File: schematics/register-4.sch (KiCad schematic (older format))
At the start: 0 parts

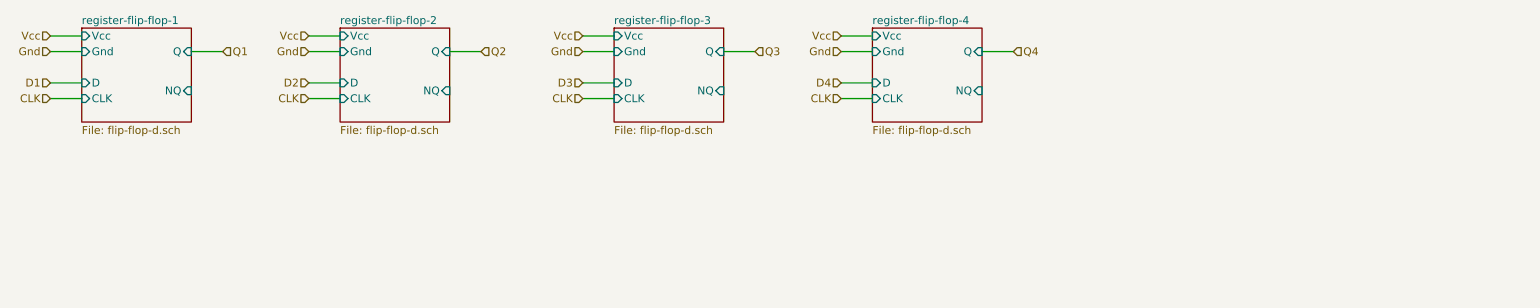
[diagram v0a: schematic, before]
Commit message: Fleshes out basic schematics and some utility software
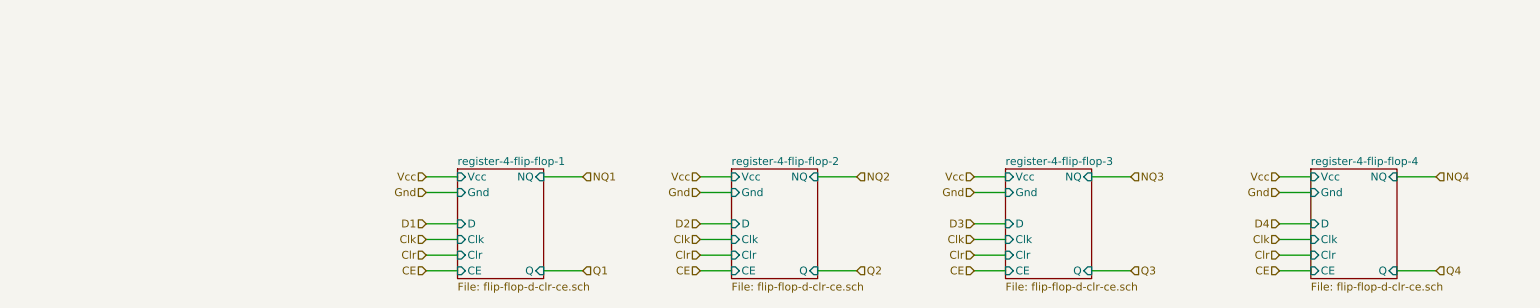
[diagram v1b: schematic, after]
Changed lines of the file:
@@
 $Descr A4 11693 8268
 encoding utf-8
-Sheet 58 225
+Sheet 14 50
 Title ""
 Date ""
@@
 $EndDescr
 $Sheet
-S 1450 2000 700  600
-U 5C3B86A2
-F0 "register-flip-flop-1" 50
-F1 "flip-flop-d.sch" 50
-F2 "Vcc" I L 1450 2050 50
-F3 "Gnd" I L 1450 2150 50
-F4 "D" I L 1450 2350 50
-F5 "CLK" I L 1450 2450 50
-F6 "Q" I R 2150 2150 50
-F7 "NQ" I R 2150 2400 50
+S 3850 2900 550  700
+U 5C431DC8
+F0 "register-4-flip-flop-1" 50
+F1 "flip-flop-d-clr-ce.sch" 50
+F2 "Vcc" I L 3850 2950 50
+F3 "Gnd" I L 3850 3050 50
+F4 "D" I L 3850 3250 50
+F5 "Clk" I L 3850 3350 50
+F6 "Clr" I L 3850 3450 50
+F7 "CE" I L 3850 3550 50
+F8 "Q" I R 4400 3550 50
+F9 "NQ" I R 4400 2950 50
 $EndSheet
-$Sheet
-S 3100 2000 700  600
-U 5C3B86AB
-F0 "register-flip-flop-2" 50
-F1 "flip-flop-d.sch" 50
-F2 "Vcc" I L 3100 2050 50
-F3 "Gnd" I L 3100 2150 50
-F4 "D" I L 3100 2350 50
-F5 "CLK" I L 3100 2450 50
-F6 "Q" I R 3800 2150 50
-F7 "NQ" I R 3800 2400 50
-$EndSheet
-$Sheet
-S 4850 2000 700  600
-U 5C3B86B4
-F0 "register-flip-flop-3" 50
-F1 "flip-flop-d.sch" 50
-F2 "Vcc" I L 4850 2050 50
-F3 "Gnd" I L 4850 2150 50
-F4 "D" I L 4850 2350 50
-F5 "CLK" I L 4850 2450 50
-F6 "Q" I R 5550 2150 50
-F7 "NQ" I R 5550 2400 50
-$EndSheet
-$Sheet
-S 6500 2000 700  600
-U 5C3B86BD
-F0 "register-flip-flop-4" 50
-F1 "flip-flop-d.sch" 50
-F2 "Vcc" I L 6500 2050 50
-F3 "Gnd" I L 6500 2150 50
-F4 "D" I L 6500 2350 50
-F5 "CLK" I L 6500 2450 50
-F6 "Q" I R 7200 2150 50
-F7 "NQ" I R 7200 2400 50
-$EndSheet
-Text HLabel 1250 2050 0    50   Input ~ 0
+Text HLabel 3650 2950 0    50   Input ~ 0
 Vcc
-Text HLabel 1250 2150 0    50   Input ~ 0
+Text HLabel 3650 3050 0    50   Input ~ 0
 Gnd
 Wire Wire Line
-	1250 2050 1450 2050
+	3650 2950 3850 2950
 Wire Wire Line
-	1250 2150 1450 2150
-Text HLabel 2900 2050 0    50   Input ~ 0
+	3650 3050 3850 3050
+Text HLabel 3650 3250 0    50   Input ~ 0
+D1
+Wire Wire Line
+	3650 3350 3850 3350
+Wire Wire Line
+	3650 3450 3850 3450
+Wire Wire Line
+	3650 3550 3850 3550
+Wire Wire Line
+	3650 3250 3850 3250
+$Sheet
+S 5600 2900 550  700
+U 5C432023
+F0 "register-4-flip-flop-2" 50
+F1 "flip-flop-d-clr-ce.sch" 50
+F2 "Vcc" I L 5600 2950 50
+F3 "Gnd" I L 5600 3050 50
+F4 "D" I L 5600 3250 50
+F5 "Clk" I L 5600 3350 50
+F6 "Clr" I L 5600 3450 50
+F7 "CE" I L 5600 3550 50
+F8 "Q" I R 6150 3550 50
+F9 "NQ" I R 6150 2950 50
+$EndSheet
+Text HLabel 5400 2950 0    50   Input ~ 0
 Vcc
-Text HLabel 2900 2150 0    50   Input ~ 0
+Text HLabel 5400 3050 0    50   Input ~ 0
 Gnd
 Wire Wire Line
-	2900 2050 3100 2050
+	5400 2950 5600 2950
 Wire Wire Line
-	2900 2150 3100 2150
-Text HLabel 4650 2050 0    50   Input ~ 0
+	5400 3050 5600 3050
+Text HLabel 5400 3250 0    50   Input ~ 0
+D2
+Wire Wire Line
+	5400 3250 5600 3250
+$Sheet
+S 7350 2900 550  700
+U 5C432127
+F0 "register-4-flip-flop-3" 50
+F1 "flip-flop-d-clr-ce.sch" 50
+F2 "Vcc" I L 7350 2950 50
+F3 "Gnd" I L 7350 3050 50
+F4 "D" I L 7350 3250 50
+F5 "Clk" I L 7350 3350 50
+F6 "Clr" I L 7350 3450 50
+F7 "CE" I L 7350 3550 50
+F8 "Q" I R 7900 3550 50
+F9 "NQ" I R 7900 2950 50
+$EndSheet
+Text HLabel 7150 2950 0    50   Input ~ 0
 Vcc
-Text HLabel 4650 2150 0    50   Input ~ 0
+Text HLabel 7150 3050 0    50   Input ~ 0
 Gnd
 Wire Wire Line
-	4650 2050 4850 2050
+	7150 2950 7350 2950
 Wire Wire Line
-	4650 2150 4850 2150
-Text HLabel 6300 2050 0    50   Input ~ 0
+	7150 3050 7350 3050
+Text HLabel 7150 3250 0    50   Input ~ 0
+D3
+Wire Wire Line
+	7150 3250 7350 3250
+$Sheet
+S 9300 2900 550  700
+U 5C4322A0
+F0 "register-4-flip-flop-4" 50
+F1 "flip-flop-d-clr-ce.sch" 50
+F2 "Vcc" I L 9300 2950 50
+F3 "Gnd" I L 9300 3050 50
+F4 "D" I L 9300 3250 50
+F5 "Clk" I L 9300 3350 50
+F6 "Clr" I L 9300 3450 50
+F7 "CE" I L 9300 3550 50
+F8 "Q" I R 9850 3550 50
+F9 "NQ" I R 9850 2950 50
+$EndSheet
+Text HLabel 9100 2950 0    50   Input ~ 0
 Vcc
-Text HLabel 6300 2150 0    50   Input ~ 0
+Text HLabel 9100 3050 0    50   Input ~ 0
 Gnd
 Wire Wire Line
-	6300 2050 6500 2050
+	9100 2950 9300 2950
 Wire Wire Line
-	6300 2150 6500 2150
-Text HLabel 1250 2350 0    50   Input ~ 0
-D1
-Text HLabel 1250 2450 0    50   Input ~ 0
-CLK
+	9100 3050 9300 3050
+Text HLabel 9100 3250 0    50   Input ~ 0
+D4
 Wire Wire Line
-	1250 2350 1450 2350
+	9100 3250 9300 3250
+Text HLabel 3650 3350 0    50   Input ~ 0
+Clk
+Text HLabel 3650 3450 0    50   Input ~ 0
+Clr
+Text HLabel 3650 3550 0    50   Input ~ 0
+CE
 Wire Wire Line
-	1250 2450 1450 2450
-Text HLabel 2900 2350 0    50   Input ~ 0
-D2
-Text HLabel 2900 2450 0    50   Input ~ 0
-CLK
+	5400 3350 5600 3350
 Wire Wire Line
-	2900 2350 3100 2350
+	5400 3450 5600 3450
 Wire Wire Line
-	2900 2450 3100 2450
-Text HLabel 4650 2350 0    50   Input ~ 0
-D3
-Text HLabel 4650 2450 0    50   Input ~ 0
-CLK
+	5400 3550 5600 3550
+Text HLabel 5400 3350 0    50   Input ~ 0
+Clk
+Text HLabel 5400 3450 0    50   Input ~ 0
+Clr
+Text HLabel 5400 3550 0    50   Input ~ 0
+CE
 Wire Wire Line
-	4650 2350 4850 2350
+	7150 3350 7350 3350
 Wire Wire Line
-	4650 2450 4850 2450
-Text HLabel 6300 2350 0    50   Input ~ 0
-D4
-Text HLabel 6300 2450 0    50   Input ~ 0
-CLK
+	7150 3450 7350 3450
 Wire Wire Line
-	6300 2350 6500 2350
+	7150 3550 7350 3550
+Text HLabel 7150 3350 0    50   Input ~ 0
+Clk
+Text HLabel 7150 3450 0    50   Input ~ 0
+Clr
+Text HLabel 7150 3550 0    50   Input ~ 0
+CE
 Wire Wire Line
-	6300 2450 6500 2450
-Text HLabel 2350 2150 2    50   Input ~ 0
+	9100 3350 9300 3350
+Wire Wire Line
+	9100 3450 9300 3450
+Wire Wire Line
+	9100 3550 9300 3550
+Text HLabel 9100 3350 0    50   Input ~ 0
+Clk
+Text HLabel 9100 3450 0    50   Input ~ 0
+Clr
+Text HLabel 9100 3550 0    50   Input ~ 0
+CE
+Text HLabel 6400 3550 2    50   Input ~ 0
+Q2
+Text HLabel 6400 2950 2    50   Input ~ 0
+NQ2
+Wire Wire Line
+	6400 2950 6150 2950
+Wire Wire Line
+	6400 3550 6150 3550
+Text HLabel 8150 3550 2    50   Input ~ 0
+Q3
+Text HLabel 8150 2950 2    50   Input ~ 0
+NQ3
+Wire Wire Line
+	8150 2950 7900 2950
+Wire Wire Line
+	8150 3550 7900 3550
+Text HLabel 10100 3550 2    50   Input ~ 0
+Q4
+Text HLabel 10100 2950 2    50   Input ~ 0
+NQ4
+Wire Wire Line
+	10100 2950 9850 2950
+Wire Wire Line
+	10100 3550 9850 3550
+Text HLabel 4650 3550 2    50   Input ~ 0
 Q1
+Text HLabel 4650 2950 2    50   Input ~ 0
+NQ1
 Wire Wire Line
-	2350 2150 2150 2150
-Text HLabel 4000 2150 2    50   Input ~ 0
-Q2
+	4650 2950 4400 2950
 Wire Wire Line
-	4000 2150 3800 2150
-Text HLabel 5750 2150 2    50   Input ~ 0
-Q3
-Wire Wire Line
-	5750 2150 5550 2150
-Text HLabel 7400 2150 2    50   Input ~ 0
-Q4
-Wire Wire Line
-	7400 2150 7200 2150
+	4650 3550 4400 3550
 $EndSCHEMATC
